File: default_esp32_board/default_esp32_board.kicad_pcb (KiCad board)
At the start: 2 copper layers, 68 x 82 mm, 60 parts, among them IC1 TPS56339DDCR, IC2 TPS56339DDCR, J10 5V_T1, J3 Pwr, J4 Conn_01x15_Socket, J5 ZED_F9P_MOD, J6 Conn_01x15_Socket, J7 5V_T1, J8 3V3_T2, J9 3V3_T1

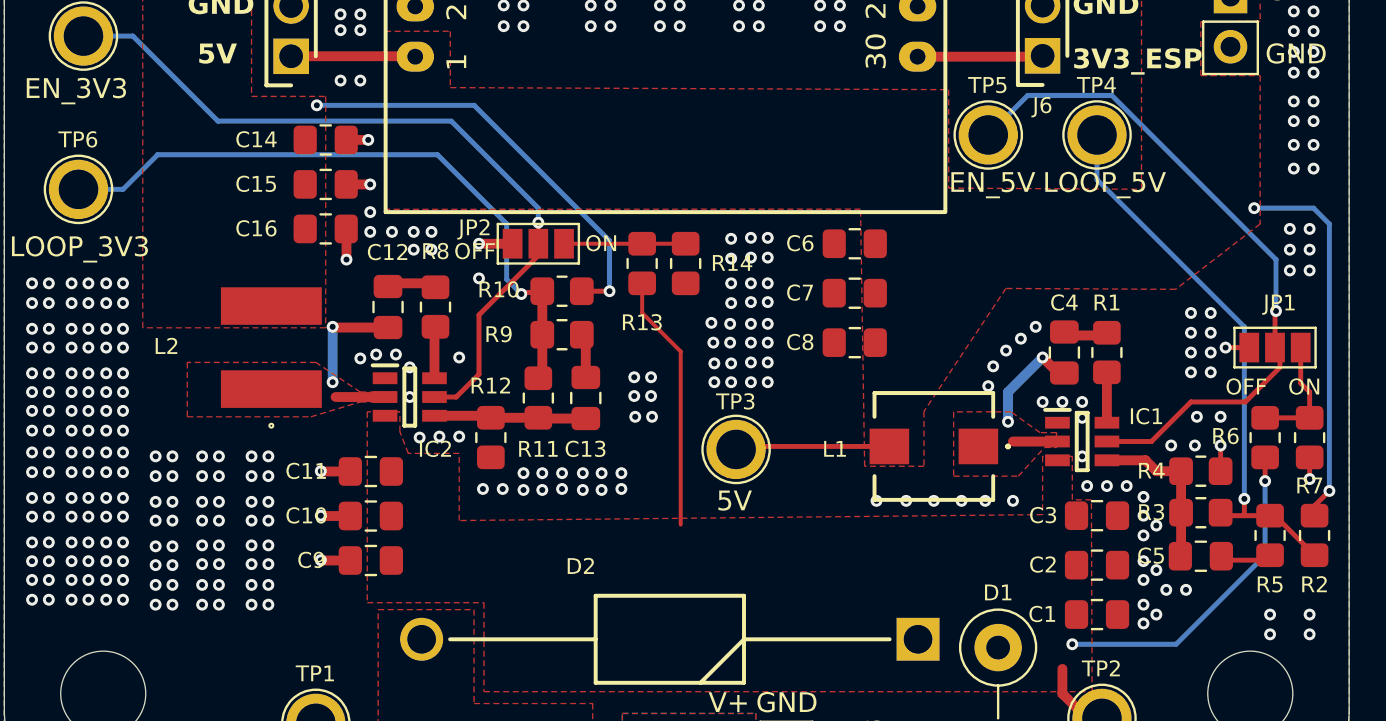
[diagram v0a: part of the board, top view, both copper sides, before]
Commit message: Changed bad ESP32 30 pin footprint, changed bucks footprints to make it easier to solder in the new version
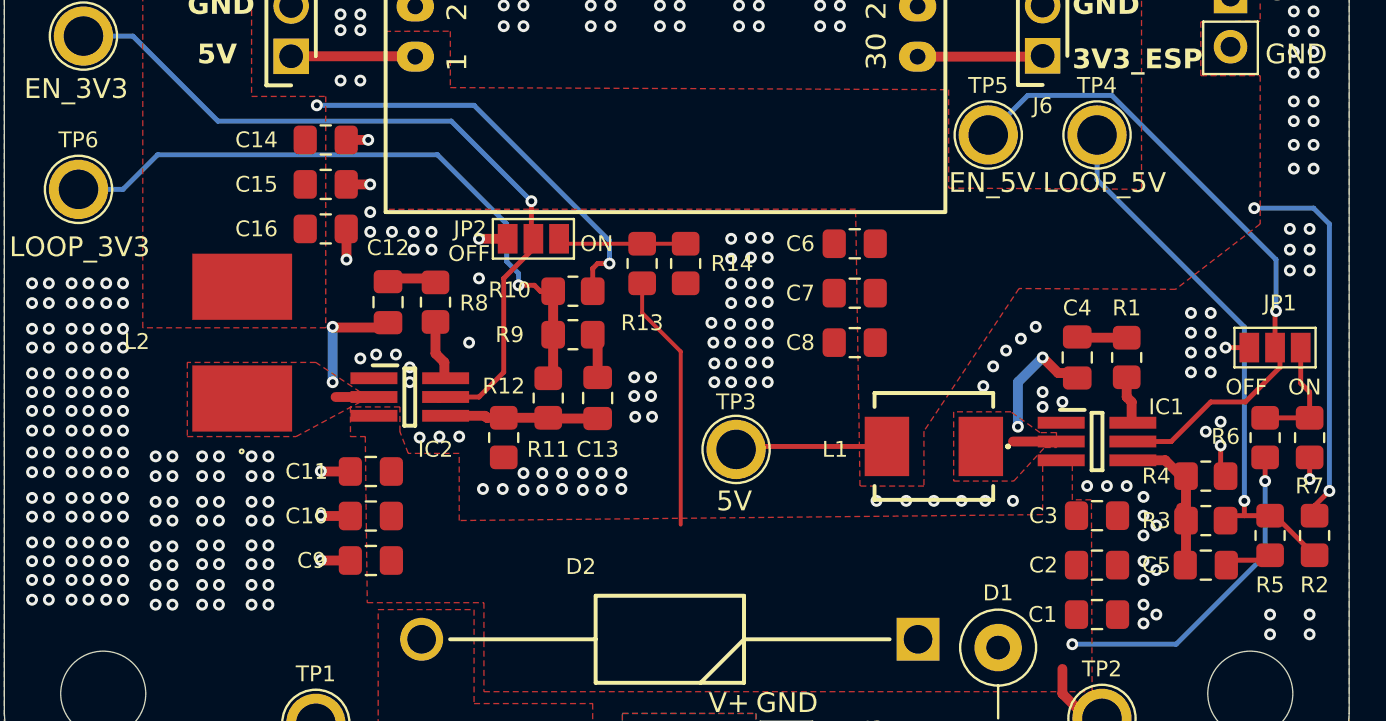
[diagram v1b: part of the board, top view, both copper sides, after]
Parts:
- IC1, IC2: value TPS56339DDCR -> SOT95P280X110-6N
- moved L2 1.52 mm to (92.0, 102.0)
- moved R1 1.03 mm to (136.8, 102.8)
- moved IC1 0.75 mm to (135.2, 107.0)
- moved C4 0.70 mm to (134.2, 102.8)
- moved R12 0.65 mm to (105.2, 106.8)
- moved C13 0.60 mm to (110.0, 104.8)
- moved R10 0.55 mm to (108.8, 99.4)
- moved R9 0.55 mm to (108.8, 101.6)
- moved C5 0.51 mm to (140.8, 113.2)
- moved R11 0.50 mm to (107.5, 104.8)
- moved R3 0.47 mm to (140.8, 111.0)
- moved JP2 0.35 mm to (106.8, 96.8)
- moved R4 0.35 mm to (140.8, 108.8)
- moved C12 0.25 mm to (99.4, 100.0)
- moved R8 0.25 mm to (101.8, 100.0)
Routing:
- net Net-(IC1-FB): track 8.29 -> 10.4 mm
- net SW: track 7.65 -> 8.64 mm
- net EN: track 34.7 -> 33.9 mm
- net 3V3: track 25.6 -> 24.9 mm
- net Net-(IC2-FB): track 7.71 -> 8.31 mm
- net GND: track 13.7 -> 13.8 mm, vias 562 -> 556
